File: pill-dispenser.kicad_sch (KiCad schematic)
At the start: 1 part

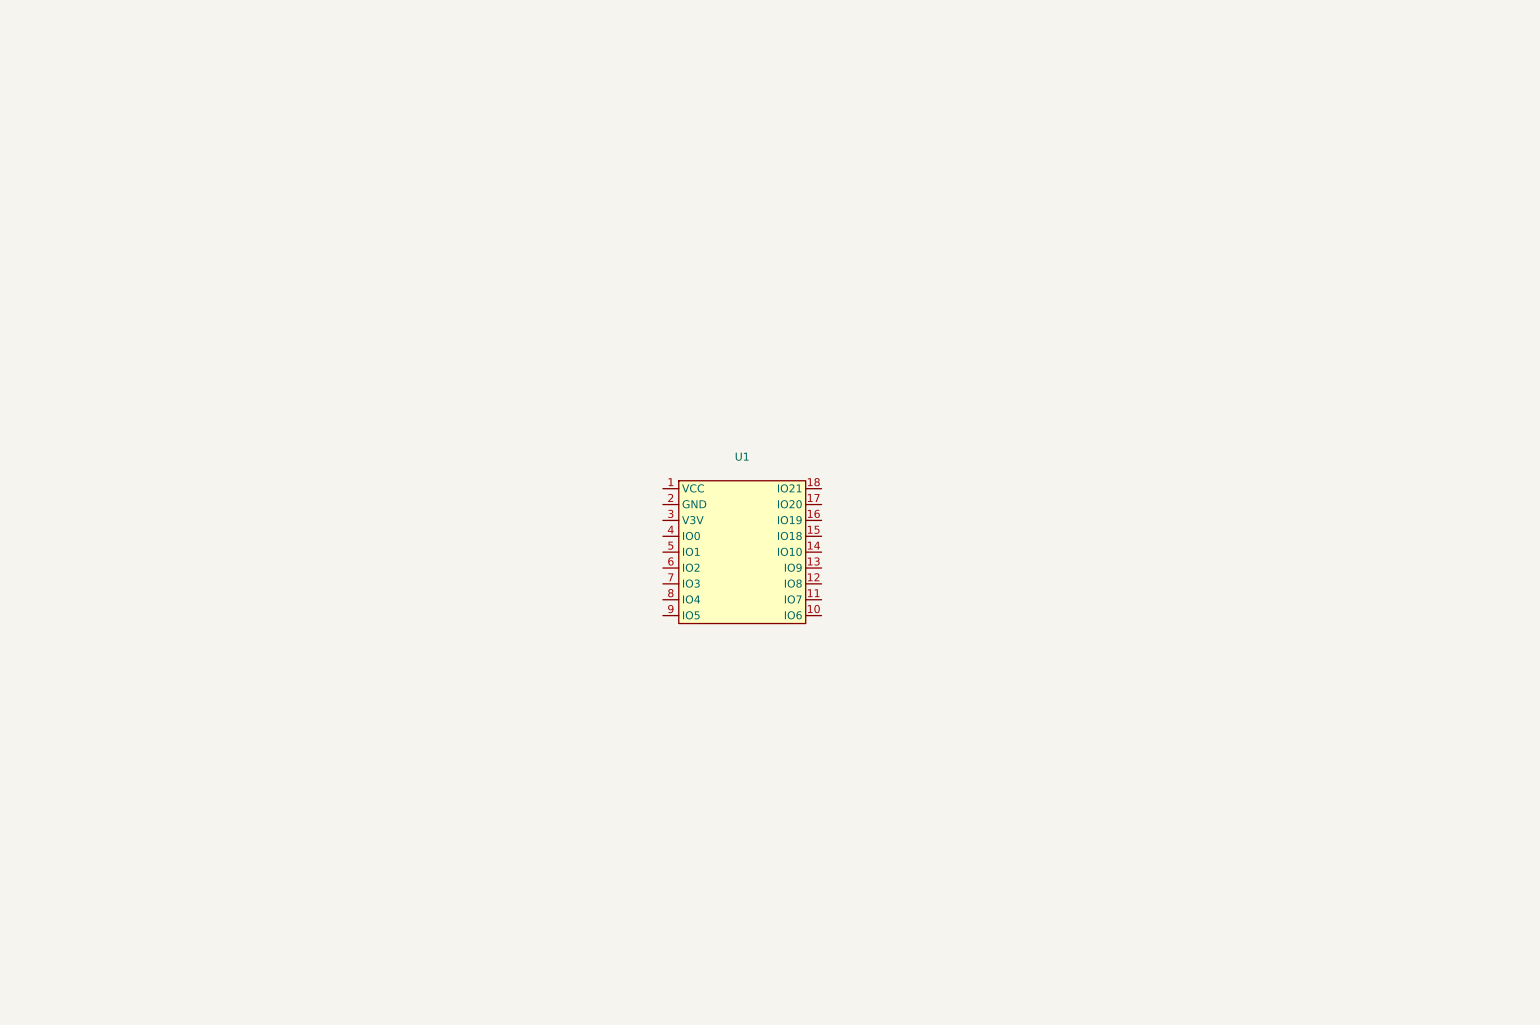
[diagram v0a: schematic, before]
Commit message: Created pill-dispenser schematic
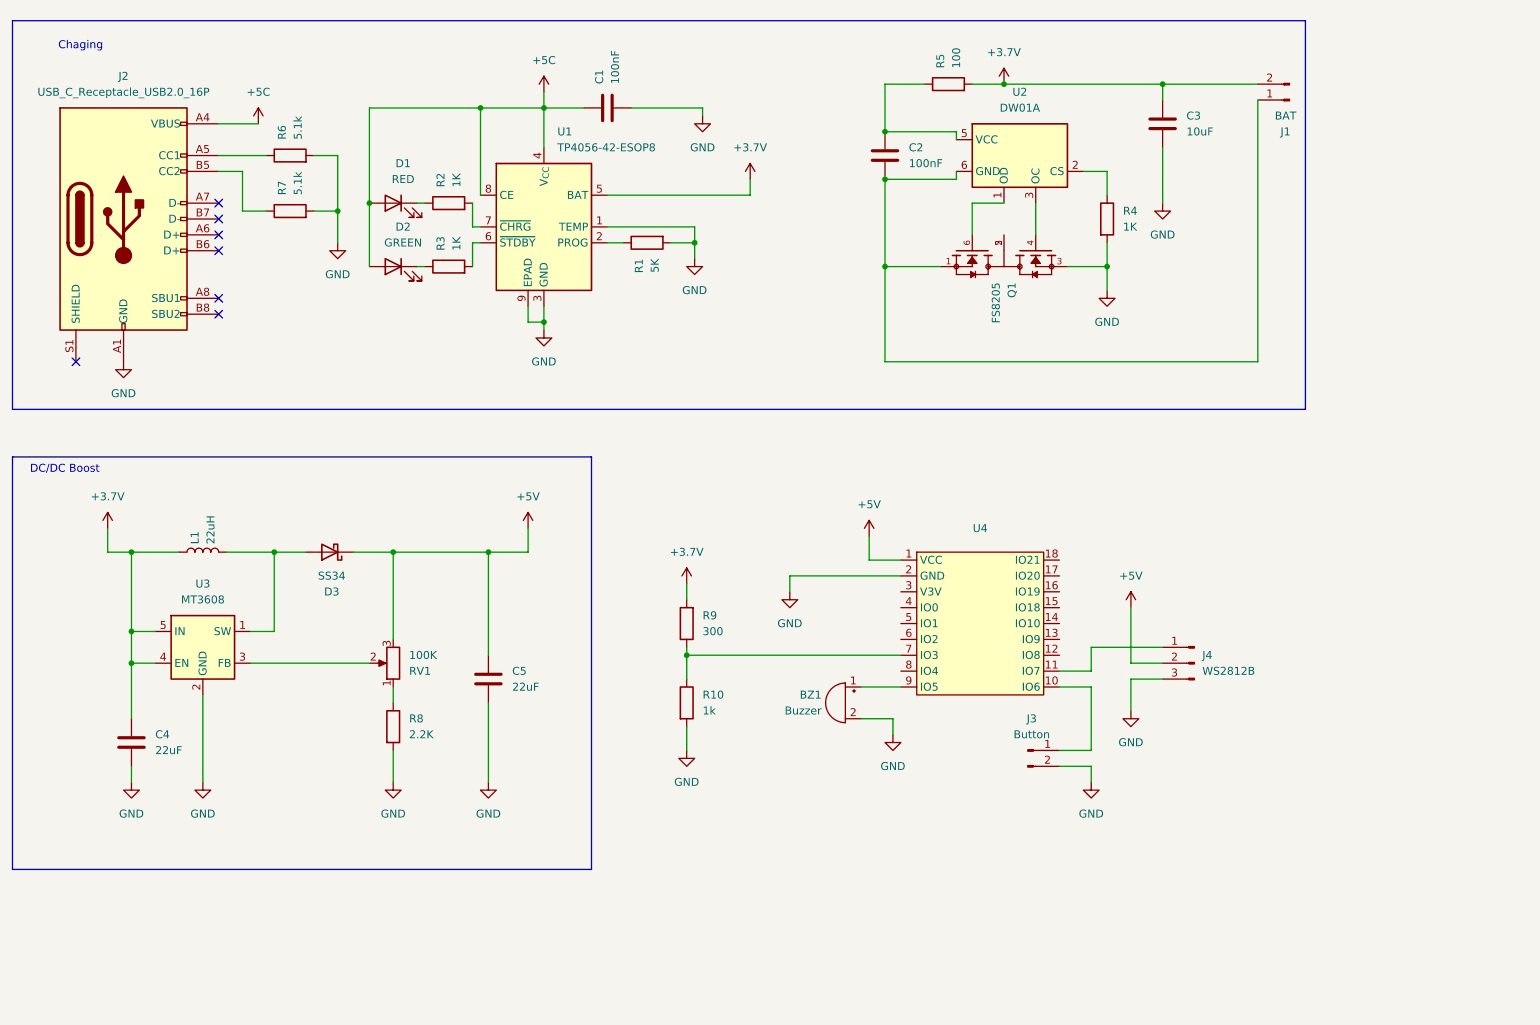
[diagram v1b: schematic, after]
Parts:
- removed U1: ~, Waveshare-ESP32:Waveshare-ESP32-C3-Zero, symbol Waveshare-ESP32:Waveshare-ESP32-C3-Zero
- added BZ1: Buzzer, symbol Device:Buzzer
- added C1, C2: 100nF, symbol Device:C
- added C3: 10uF, symbol Device:C
- added C4, C5: 22uF, symbol Device:C
- added D1: RED, symbol Device:LED
- added D2: GREEN, symbol Device:LED
- added D3: SS34, Diode_SMD:D_SMA, symbol Diode:SS34
- added J1: BAT, symbol Connector:Conn_01x02_Pin
- added J2: USB_C_Receptacle_USB2.0_16P, symbol Connector:USB_C_Receptacle_USB2.0_16P
- added J3: Button, symbol Connector:Conn_01x02_Pin
- added J4: WS2812B, symbol Connector:Conn_01x03_Pin
- added L1: 22uH, symbol Device:L
- added Q1: FS8205, FS8205:SOT95P280X145-6N, symbol FS8205:FS8205
- added R1: 5K, symbol Device:R
- added R10: 1k, symbol Device:R
- added R2, R3, R4: 1K, symbol Device:R
- added R5: 100, symbol Device:R
- added R6, R7: 5.1k, symbol Device:R
- added R8: 2.2K, symbol Device:R
- added R9: 300, symbol Device:R
- added RV1: 100K, symbol Device:R_Potentiometer
- added U1: TP4056-42-ESOP8, Package_SO:SOIC-8-1EP_3.9x4.9mm_P1.27mm_EP2.41x3.3mm_ThermalVias, symbol Battery_Management:TP4056-42-ESOP8
- added U2: DW01A, Package_TO_SOT_SMD:SOT-23-6, symbol Battery_Management:DW01A
- added U3: MT3608, Package_TO_SOT_SMD:SOT-23-6, symbol Regulator_Switching:MT3608
- added U4: ~, Waveshare-ESP32:Waveshare-ESP32-C3-Zero, symbol Waveshare-ESP32:Waveshare-ESP32-C3-Zero
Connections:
- new net: R1.1, U1.2 (PROG)
- new net: R3.2, U1.6 (~{STDBY})
- new net: R2.2, U1.7 (~{CHRG})
- new net: J2.A5 (CC1), R6.1
- new net: D3.2 (A), L1.2, U3.1 (SW)
- new net: RV1.2, U3.3 (FB)
- new net: J2.B5 (CC2), R7.1
- new net: R4.1, U2.2 (CS)
- new net: C2.2, J1.1 (Pin_1), Q1.1, U2.6 (GND)
- new net: Q1.2, Q1.5
- new net: Q1.4, U2.3 (OC)
- new net: Q1.6, U2.1 (OD)
- new net: J3.1 (Pin_1), U4.10 (IO6)
- new net: C2.1, R5.1, U2.5 (VCC)
- new net: BZ1.1 (+), U4.9 (IO5)
- new net: R8.1, RV1.1
- new net: J4.1 (Pin_1), U4.11 (IO7)
- new net: D1.1 (K), R2.1
- new net: D2.1 (K), R3.1
- new net: R10.1, R9.1, U4.7 (IO3)
- new net +3.7V: C3.1, C4.1, J1.2 (Pin_2), L1.1, R5.2, R9.2, U1.5 (BAT), U3.4 (EN), U3.5 (IN)
- new net +5C: C1.1, D1.2 (A), D2.2 (A), J2.A4 (VBUS), J2.A9 (VBUS), J2.B4 (VBUS), J2.B9 (VBUS), U1.4 (V_{CC}), U1.8 (CE)
- new net +5V: C5.1, D3.1 (K), J4.2 (Pin_2), RV1.3, U4.1 (VCC)
- new net GND: BZ1.2 (-), C1.2, C3.2, C4.2, C5.2, J2.A1 (GND), J2.A12 (GND), J2.B1 (GND), J2.B12 (GND), J3.2 (Pin_2), J4.3 (Pin_3), Q1.3, R1.2, R10.2, R4.2, R6.2, R7.2, R8.2, U1.1 (TEMP), U1.3 (GND), U1.9 (EPAD), U3.2 (GND), U4.2 (GND)
- no-connect marks 0 -> 7
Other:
- note added: "Chaging"
- note added: "DC/DC Boost"

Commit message: Finished schematic
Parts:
- removed C2: 100nF, symbol Device:C
- removed C3: 10uF, symbol Device:C
- removed J1: BAT, symbol Connector:Conn_01x02_Pin
- removed Q1: FS8205, FS8205:SOT95P280X145-6N, symbol FS8205:FS8205
- removed R5: 100, symbol Device:R
- removed RV1: 100K, symbol Device:R_Potentiometer
- removed U2: DW01A, Package_TO_SOT_SMD:SOT-23-6, symbol Battery_Management:DW01A
- added C4: 0.1u, symbol Device:C
- added D2: MBR0520, Diode_SMD:D_SOD-123, symbol Diode:MBR0520
- added J2: BAT, symbol Connector:Conn_01x02_Pin
- added Q1: AO3401A, Package_TO_SOT_SMD:SOT-23, symbol Transistor_FET:AO3401A
- added Q2: FS8205A, FS8205A:SOP65P640X120-8N, symbol FS8205A:FS8205A
- added R1: 75К, symbol Device:R
- added R12: 1K, symbol Device:R
- added R7: 100, symbol Device:R
- added U4: DW01A, Package_TO_SOT_SMD:SOT-23-6, symbol Battery_Management:DW01A
- BZ1: footprint (none) -> Buzzer_Beeper:Indicator_PUI_AI-1440-TWT-24V-2-R; CHIPDIP (none) -> https://www.chipdip.ru/product/hpm14a
- C3: renamed from C1; value 100nF -> 10uF
- D1: renamed from D3; CHIPDIP (none) -> https://www.chipdip.ru/product/ss34-umw
- J1: renamed from J2; value USB_C_Receptacle_USB2.0_16P -> USB-C; footprint (none) -> Connector_USB:USB_C_Plug_JAE_DX07P024AJ1; CHIPDIP (none) -> https://www.chipdip.ru/product0/8008927423
- R4: value 1K -> 100k
- R5: renamed from R8; value 2.2K -> 10K
- U3: renamed from U1; footprint Package_SO:SOIC-8-1EP_3.9x4.9mm_P1.27mm_EP2.41x3.3mm_ThermalVias -> TP4056-42-ESOP8:SOIC127P600X175-9N; CHIPDIP (none) -> https://www.chipdip.ru/product/tp4056-42-sop8-pp
- renumbered C5 to C1, C4 to C2, D1 to D3, D2 to D4, R1 to R10, R10 to R11, R7 to R2, R6 to R3, R2 to R6, R9 to R8, R3 to R9, U3 to U1, U4 to U2
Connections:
- net +5C is gone; now on net VUSB: C3.1, D3.2 (A), D4.2 (A), J1.A4 (VBUS), J1.A9 (VBUS), J1.B4 (VBUS), J1.B9 (VBUS), U3.4 (V_{CC}), U3.8 (CE)
- net +5V: now also J4.1 (Pin_1), R1.1; no longer J4.2 (Pin_2)
- net GND: now also J1.S1 (SHIELD), R10.1, R2.1, R3.1, Q2.6, Q2.7, R12.2; no longer R10.2, R2.2, R3.2
- net at U3.2 (PROG): now also R10.2; no longer R10.1
- net at J1.A5 (CC1): now also R3.2; no longer R3.1
- net at U1.3 (FB): now also R5.1, R1.2
- net at J1.B5 (CC2): now also R2.2; no longer R2.1
- net VUSB: now reaches R4.1
- net VUSB: now also D2.2 (A), Q1.1 (G)
- net BUTTON: now reaches J3.1 (Pin_1), U2.10 (IO6)
- net BUZ: now reaches BZ1.1 (+), U2.9 (IO5)
- net at U2.11 (IO7): no longer J4.1 (Pin_1)
- net LED_STRIP: now reaches U2.12 (IO8)
- net LED_STRIP: now also J4.2 (Pin_2)
- net BAT_MON: now reaches R11.1, R8.1, U2.7 (IO3)
- net +3.7V: no longer names the net of C2.1, L1.1, U1.4 (EN), U1.5 (IN)
- net +3.7V: now also D2.1 (K), Q1.2 (S); no longer R8.2, U3.5 (BAT)
- new net: Q2.1, Q2.8
- new net: C4.2, J2.B- (Pin_1), Q2.2, Q2.3, U4.6 (GND)
- new net: Q2.4, U4.1 (OD)
- new net: Q2.5, U4.3 (OC)
- new net: R12.1, U4.2 (CS)
- new net: C4.1, R7.1, U4.5 (VCC)
- new net VBAT: J2.B+ (Pin_2), Q1.3 (D), R7.2, R8.2, U3.5 (BAT)
- no-connect marks 7 -> 19
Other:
- note removed: "Chaging"
- note removed: "DC/DC Boost"
- moved on the sheet: BZ1, C1, C2, C3, D1, D3, D4, J1, J3, J4, L1, R10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

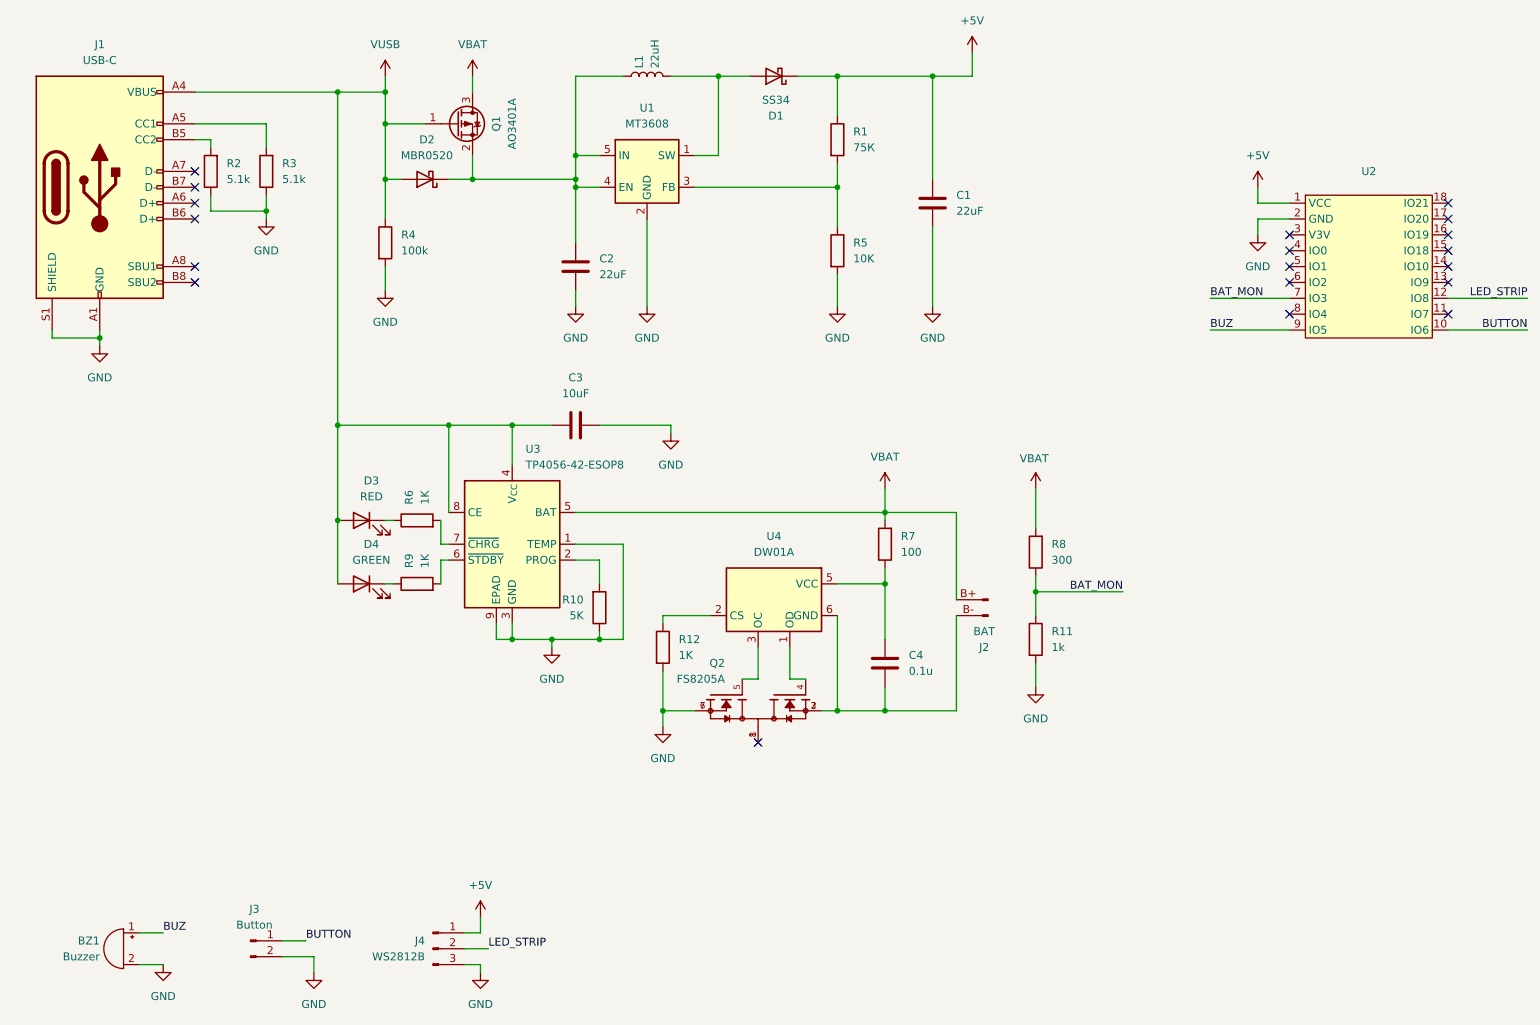
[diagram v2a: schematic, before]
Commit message: Finished schematic and prepare for PCB layout
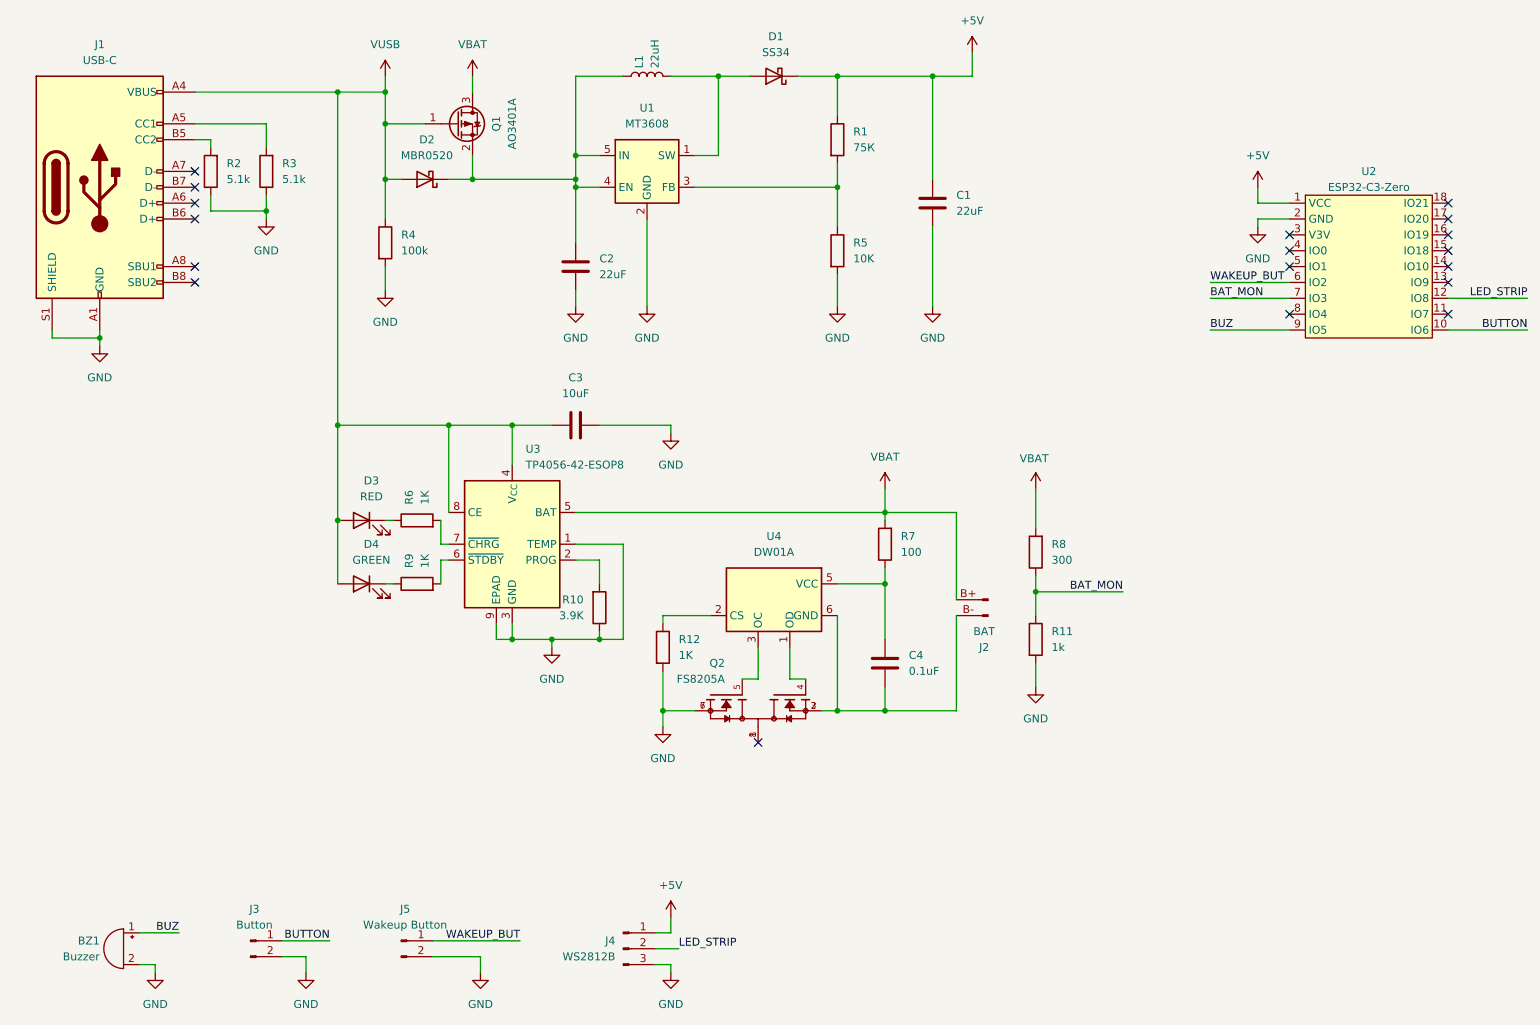
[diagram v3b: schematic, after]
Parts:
- added J5: Wakeup Button, Connector_PinSocket_2.54mm:PinSocket_1x02_P2.54mm_Horizontal, symbol Connector:Conn_01x02_Pin
- C1, C2: footprint (none) -> Capacitor_SMD:C_1206_3216Metric; CHIPDIP (none) -> https://www.chipdip.ru/product/grm31cr61c226ke15l
- C3: footprint (none) -> Capacitor_SMD:C_0805_2012Metric; CHIPDIP (none) -> https://www.chipdip.ru/product/grm21br60j106k
- C4: value 0.1u -> 0.1uF; footprint (none) -> Capacitor_SMD:C_0402_1005Metric; CHIPDIP (none) -> https://www.chipdip.ru/product0/9001068440
- D2: CHIPDIP (none) -> https://www.chipdip.ru/product/mbr0520
- D3: footprint (none) -> LS-T676-Q1R2-1-Z:LED_LG_T671-L2N1-1-Z; CHIPDIP (none) -> https://www.chipdip.ru/product0/8026991192
- D4: footprint (none) -> LED_SMD:LED_1206_3216Metric; CHIPDIP (none) -> https://www.chipdip.ru/product0/8021501452
- J2, J3: footprint (none) -> Connector_PinSocket_2.54mm:PinSocket_1x02_P2.54mm_Horizontal
- J4: footprint (none) -> Connector_PinSocket_2.54mm:PinSocket_1x03_P2.54mm_Horizontal
- L1: footprint (none) -> Inductor_SMD:L_1210_3225Metric; CHIPDIP (none) -> https://www.chipdip.ru/product/nlcv32t-220k-ef-22
- R1: footprint (none) -> Resistor_SMD:R_2512_6332Metric; CHIPDIP (none) -> https://www.chipdip.ru/product/1w-2512-75-kom-1
- R10: value 5K -> 3.9K; footprint (none) -> Resistor_SMD:R_2512_6332Metric; CHIPDIP (none) -> https://www.chipdip.ru/product/1w-2512-3.9-kom-5
- R11, R12, R6, R9: footprint (none) -> Resistor_SMD:R_2512_6332Metric; CHIPDIP (none) -> https://www.chipdip.ru/product/1w-2512-1-kom-1
- R2, R3: footprint (none) -> Resistor_SMD:R_2512_6332Metric; CHIPDIP (none) -> https://www.chipdip.ru/product/1w-2512-5.1-kom-5
- R4, R5: footprint (none) -> Resistor_SMD:R_2512_6332Metric; CHIPDIP (none) -> https://www.chipdip.ru/product/1w-2512-100-kom-1
- R7: footprint (none) -> Resistor_SMD:R_2512_6332Metric; CHIPDIP (none) -> https://www.chipdip.ru/product/1w-2512-100-om-5
- R8: footprint (none) -> Resistor_SMD:R_2512_6332Metric; CHIPDIP (none) -> https://www.chipdip.ru/product/1w-2512-300-kom-1
- U2: value ~ -> ESP32-C3-Zero; footprint Waveshare-ESP32:Waveshare-ESP32-C3-Zero -> waveshare-esp32:Waveshare-ESP32-C3-Zero
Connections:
- net GND: now also J5.2 (Pin_2)
- net WAKEUP_BUT: now reaches U2.6 (IO2)
- net WAKEUP_BUT: now also J5.1 (Pin_1)
- no-connect marks 19 -> 18
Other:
- company: (none) -> TelePat, LLC
- title: (none) -> Main Board
- moved on the sheet: J4

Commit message: Created PCB layout
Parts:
- C4: footprint Capacitor_SMD:C_0402_1005Metric -> Capacitor_SMD:C_1210_3225Metric; CHIPDIP https://www.chipdip.ru/product0/9001068440 -> https://www.chipdip.ru/product/cc1210kkx7r9bb104
- J1: footprint Connector_USB:USB_C_Plug_JAE_DX07P024AJ1 -> Connector_USB:USB_C_Receptacle_Palconn_UTC16-G
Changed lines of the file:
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@@
 			)
 		)
-		(property "Footprint" "Capacitor_SMD:C_0402_1005Metric"
+		(property "Footprint" "Capacitor_SMD:C_1210_3225Metric"
 			(at 157.1752 123.19 0)
 			(effects
@@
 			)
 		)
-		(property "CHIPDIP" "https://www.chipdip.ru/product0/9001068440"
+		(property "CHIPDIP" "https://www.chipdip.ru/product/cc1210kkx7r9bb104"
 			(at 156.21 119.38 0)
 			(effects
@@
 			)
 		)
-		(property "Footprint" "Connector_USB:USB_C_Plug_JAE_DX07P024AJ1"
+		(property "Footprint" "Connector_USB:USB_C_Receptacle_Palconn_UTC16-G"
 			(at 34.29 43.18 0)
 			(effects
